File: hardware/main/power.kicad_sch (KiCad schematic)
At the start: 59 parts, among them J1 USB-307HB-B-SU, J12 Interrupteur, J2 Batterie 18650, Q1 AO3401A, Q2 2N7002, U10 FS8205, U12 USBLC6-2SC6, U5 AP2112M-3.3, U6 AP2112K-3.3, U7 MT3608, U8 BQ24075RGTR, U9 DW01A

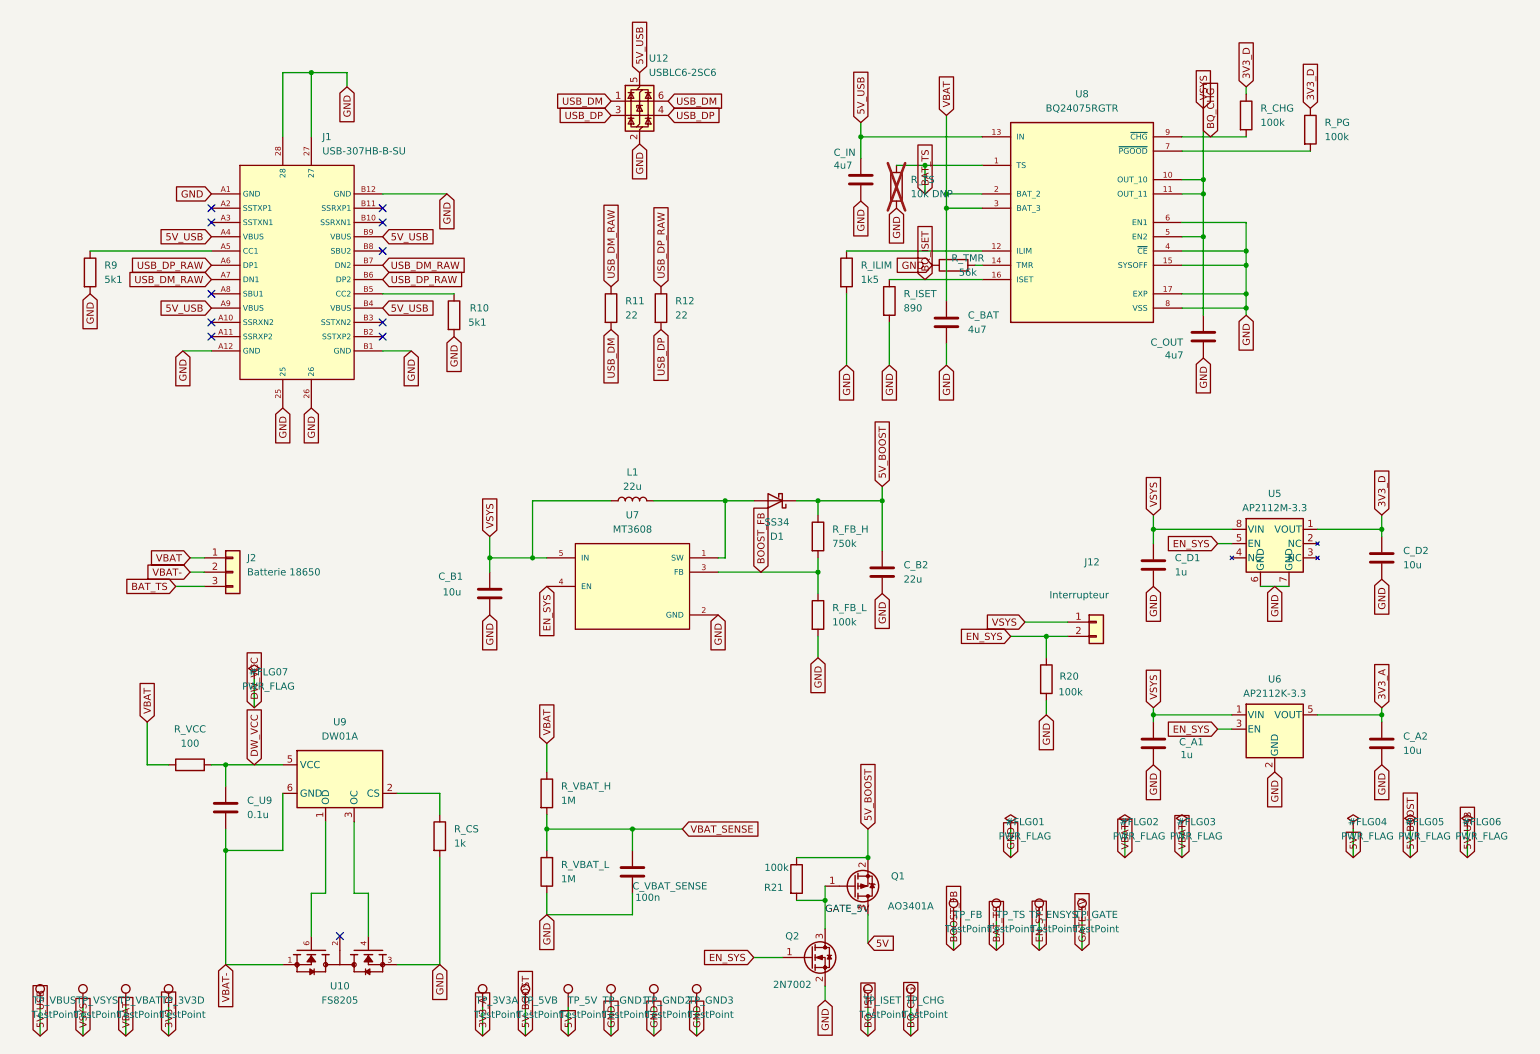
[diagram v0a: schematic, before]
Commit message: datasheets: ATtiny1616, reference documentaire non inventee
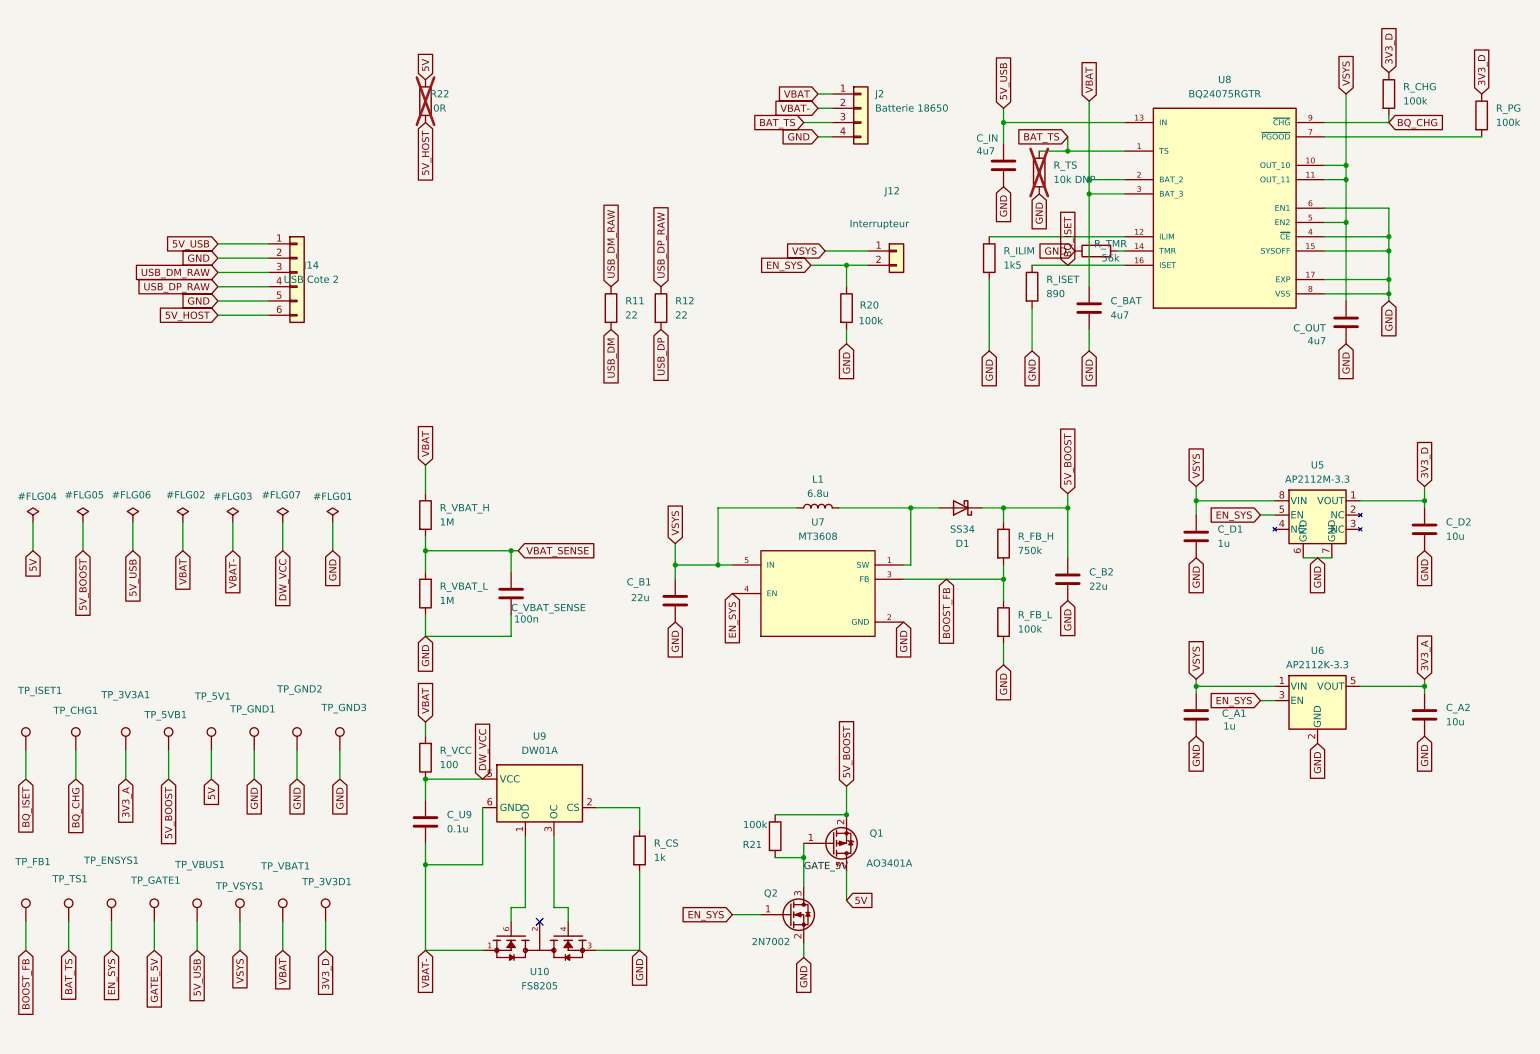
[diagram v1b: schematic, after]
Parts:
- removed J1: USB-307HB-B-SU, lcsc_footprints:C309361_USB-C-SMD_USB-307HB-B-SU, symbol lcsc_imported:USB-307HB-B-SU
- removed R10, R9: 5k1, Resistor_SMD:R_0402_1005Metric, symbol Device:R
- removed TP_3V3A, TP_3V3D, TP_5V, TP_5VB, TP_CHG, TP_ENSYS, TP_FB, TP_GATE, TP_ISET, TP_TS, TP_VBAT, TP_VBUS, TP_VSYS: TestPoint, TestPoint:TestPoint_Pad_D1.5mm, symbol Connector:TestPoint
- removed U12: USBLC6-2SC6, Package_TO_SOT_SMD:SOT-23-6, symbol Power_Protection:USBLC6-2P6
- added J14: USB Cote 2, Connector_JST:JST_PH_B6B-PH-K_1x06_P2.00mm_Vertical, symbol Connector_Generic:Conn_01x06
- added R22: 0R, Resistor_SMD:R_0603_1608Metric, symbol Device:R
- added TP_3V3A1, TP_3V3D1, TP_5V1, TP_5VB1, TP_CHG1, TP_ENSYS1, TP_FB1, TP_GATE1, TP_ISET1, TP_TS1, TP_VBAT1, TP_VBUS1, TP_VSYS1: TestPoint, TestPoint:TestPoint_Pad_D1.5mm, symbol Connector:TestPoint
- C_B1: value 10u -> 22u
- J2: footprint Connector_JST:JST_PH_B3B-PH-K_1x03_P2.00mm_Vertical -> Connector_JST:JST_PH_B4B-PH-K_1x04_P2.00mm_Vertical; symbol Connector_Generic:Conn_01x03 -> Connector_Generic:Conn_01x04
- L1: value 22u -> 6.8u; footprint Inductor_SMD:L_1210_3225Metric -> lcsc_footprints:C36411_IND-SMD_L5_0-W5_0_SWPA5040S; LCSC (none) -> C36411; MPN (none) -> SWPA5040S6R8MT; Manufacturer (none) -> Sunlord
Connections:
- net 3V3_A: now also TP_3V3A1.1
- net 3V3_D: now also TP_3V3D1.1
- net 5V: now also R22.1, TP_5V1.1
- net 5V_BOOST: now also TP_5VB1.1
- net 5V_USB: now also J14.1 (Pin_1), TP_VBUS1.1
- net BAT_TS: now also TP_TS1.1
- net BOOST_FB: now also TP_FB1.1
- net BQ_CHG: now also TP_CHG1.1
- net BQ_ISET: now also TP_ISET1.1
- net DW_VCC: now also R_VCC.1; no longer R_VCC.2
- net EN_SYS: now also TP_ENSYS1.1
- net GATE_5V: now also TP_GATE1.1
- net GND: now also J2.4 (Pin_4), J14.2 (Pin_2), J14.5 (Pin_5)
- net USB_DM_RAW: now also J14.3 (Pin_3)
- net USB_DP_RAW: now also J14.4 (Pin_4)
- net VBAT: now also R_VCC.2, TP_VBAT1.1; no longer R_VCC.1
- net VSYS: now also TP_VSYS1.1
- new net 5V_HOST: J14.6 (Pin_6), R22.2
- no-connect marks 11 -> 1
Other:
- moved on the sheet: C_A1, C_A2, C_B1, C_B2, C_BAT, C_D1, C_D2, C_IN, C_OUT, C_U9, C_VBAT_SENSE, D1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
